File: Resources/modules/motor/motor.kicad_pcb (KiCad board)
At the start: 2 copper layers, 50 x 40 mm, 16 parts, among them J1 power, J2 from switches, J3 motor, J4 towards uC, U1 L293D

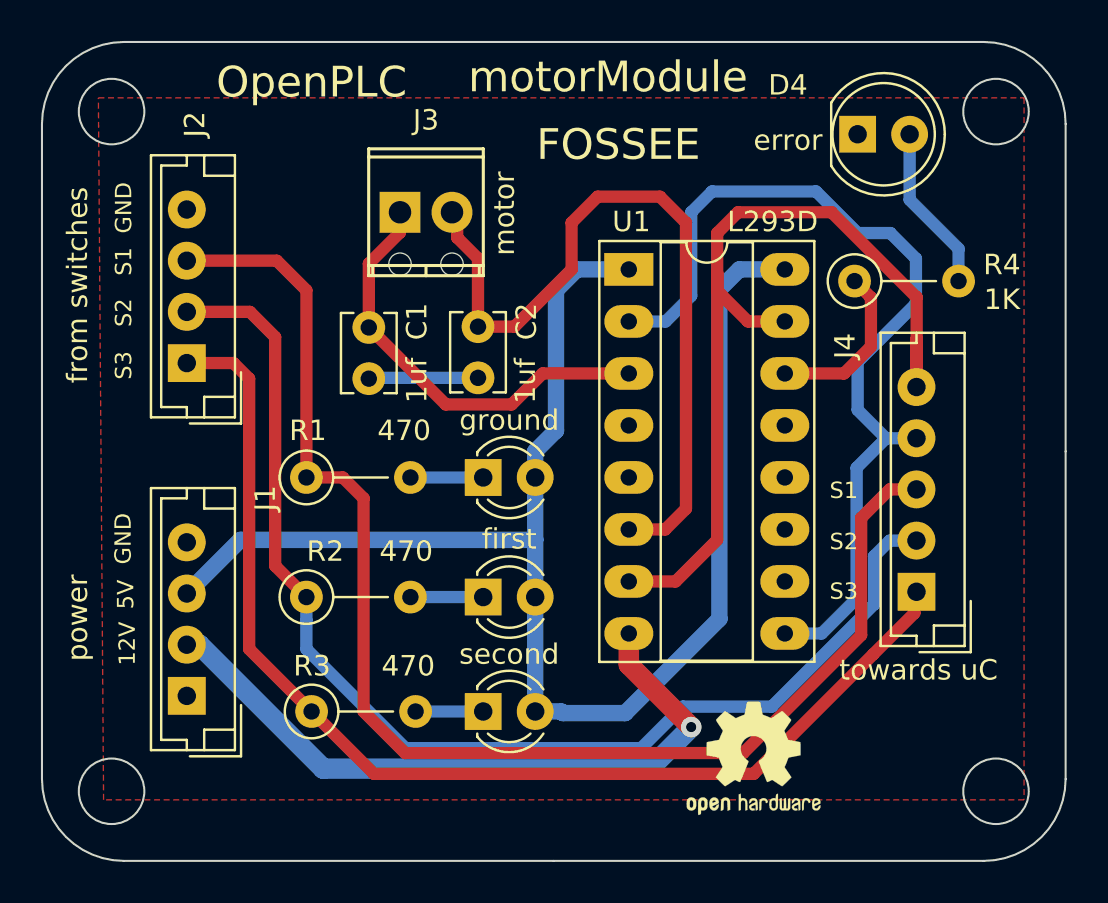
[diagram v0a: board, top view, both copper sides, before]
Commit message: Motor module: grounded 'EN3,4'; terminal connector footprint corrected; 'error led' changed to 3mm; proper footprints for 'switches' and 'towards uC' connectors; proper labelling; added 'designed using Kicad' symbol
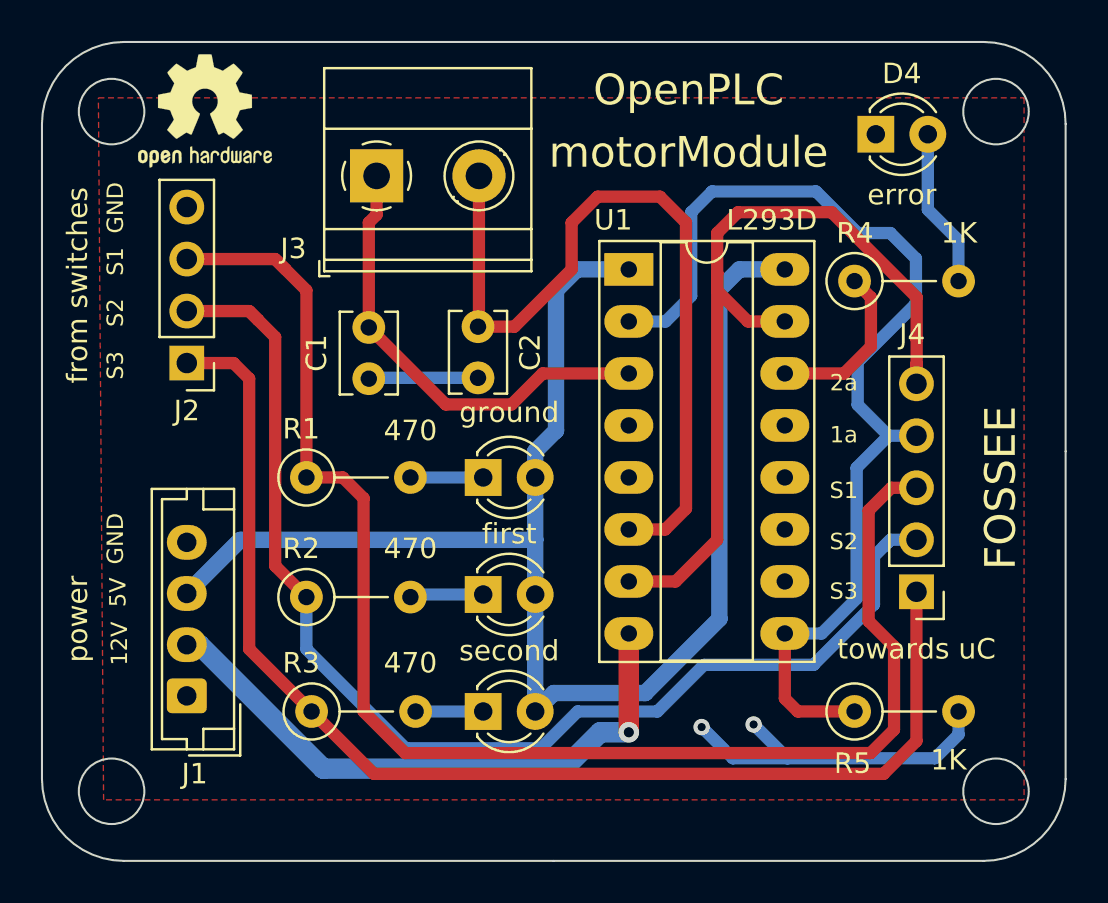
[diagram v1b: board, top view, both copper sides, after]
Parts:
- removed D2: first, LEDs:LED_D3.0mm
- removed REF***: OSHW-Logo2_7.3x6mm_SilkScreen, Symbols:OSHW-Logo2_7.3x6mm_SilkScreen
- added R5: 1K, Resistor_THT:R_Axial_DIN0207_L6.3mm_D2.5mm_P5.08mm_Vertical, F.Cu at (120.5, 112.5)
- added REF**: KiCad-Logo2_6mm_SilkScreen, Symbol:KiCad-Logo2_6mm_SilkScreen, B.Cu at (112.5, 83.8)
- added REF**: OSHW-Logo2_7.3x6mm_SilkScreen, Symbol:OSHW-Logo2_7.3x6mm_SilkScreen, F.Cu at (88.8, 83.2)
- added first: LED, LED_THT:LED_D3.0mm, F.Cu at (102.4, 106.8)
- C1, C2: footprint Capacitors_THT:C_Disc_D3.8mm_W2.6mm_P2.50mm -> Capacitor_THT:C_Disc_D3.8mm_W2.6mm_P2.50mm
- D4: footprint LEDs:LED_D5.0mm -> LED_THT:LED_D3.0mm
- J1: footprint Connectors_JST:JST_EH_B04B-EH-A_04x2.50mm_Straight -> Connector_JST:JST_EH_B4B-EH-A_1x04_P2.50mm_Vertical
- J2: footprint Connectors_JST:JST_EH_B04B-EH-A_04x2.50mm_Straight -> Connector_PinHeader_2.54mm:PinHeader_1x04_P2.54mm_Vertical
- J3: footprint TerminalBlocks_Phoenix:TerminalBlock_Phoenix_MPT-2.54mm_2pol -> TerminalBlock_Phoenix:TerminalBlock_Phoenix_MKDS-1,5-2_1x02_P5.00mm_Horizontal
- J4: footprint Connectors_JST:JST_EH_B05B-EH-A_05x2.50mm_Straight -> Connector_PinHeader_2.54mm:PinHeader_1x05_P2.54mm_Vertical
- R1, R2, R3, R4: footprint Resistors_THT:R_Axial_DIN0207_L6.3mm_D2.5mm_P5.08mm_Vertical -> Resistor_THT:R_Axial_DIN0207_L6.3mm_D2.5mm_P5.08mm_Vertical
- U1: footprint Housings_DIP:DIP-16_W7.62mm_Socket_LongPads -> Package_DIP:DIP-16_W7.62mm_Socket_LongPads
- ground: renamed from D1; value ground -> LED; footprint LEDs:LED_D3.0mm -> LED_THT:LED_D3.0mm
- second: renamed from D3; value second -> LED; footprint LEDs:LED_D3.0mm -> LED_THT:LED_D3.0mm
- moved J3 2.11 mm to (97.2, 86.4)
- moved D4 0.89 mm to (121.5, 84.3)
- turned J2 to 180 degrees
- turned J4 to 180 degrees
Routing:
- net GND: track 5.35 -> 22.5 mm, vias 0 -> 2
- net /1a: track 45.1 -> 51.9 mm
- net /sw1: track 65.7 -> 71.1 mm
- net +12V: track 33.8 -> 29.7 mm
- net /sw3: track 55.9 -> 59.8 mm
- net /2a: track 42.6 -> 41.3 mm
- net Net-(C1-Pad2): track 21.1 -> 22.4 mm
- net Net-(C2-Pad1): track 38.0 -> 39.2 mm
- net /sw2: track 58.1 -> 59.1 mm
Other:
- board text added: "1a"
- board text added: "2a"
